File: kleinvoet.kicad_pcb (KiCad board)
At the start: 4 copper layers, 123 x 66 mm, 193 parts, among them J1 Conn_ST_STDC14, J11 Micro_SD_Card_Det, J12 JST-PH, J13 USB_C_Receptacle_USB2.0, J16 GPS_Transmission_Conn, J2 FTDI_Conn, J3 Sensor_Conn, J4 GPS_Transmission_Conn, J6 Sensor_Conn, Q1 PMOS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

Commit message: Fix KICAD! & DRC
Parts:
- moved TP8 7.68 mm to (138.5, 33.2)
- moved TP7 5.06 mm to (136.5, 33.2)
- moved TP11 2.75 mm to (138.5, 35.2)
- moved C66 2.75 mm to (65.1, 50.8)
- moved C64 2.10 mm to (69.3, 50.8)
- moved CB40 2.10 mm to (77.3, 61.4)
- moved D4 2.05 mm to (64.4, 48.2)
- moved BT1 1.95 mm to (66.3, 62.5)
- moved R3 1.95 mm to (72.7, 86.2)
- moved R4 1.95 mm to (59.7, 86.2)
- moved U11 1.95 mm to (66.2, 62.2)
- moved D3 1.95 mm to (64.0, 86.2)
- moved D2 1.95 mm to (68.4, 86.2)
- moved FB10 1.95 mm to (68.1, 73.5)
- moved C65 1.90 mm to (77.2, 65.2)
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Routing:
- net /~RST: track 147.3 -> 120.9 mm, vias 5 -> 4
- net /GNSS_Module/GPS_SYNC: track 2.75 -> 28.3 mm, vias 0 -> 1
- net Earth: track 103.7 -> 82.2 mm, vias 4 -> 0
- net /GNSS_Module/GPS_RX: track 14.4 -> 34.8 mm, vias 0 -> 1
- net Net-(U11-Pad12): track 13.2 -> 0.00 mm, vias 1 -> 0
- net /A0: track 45.5 -> 34.3 mm
- net +3V3: track 57.2 -> 65.7 mm, vias 68 -> 69
- net /A4: track 39.3 -> 44.8 mm
- net Net-(BT1-Pad1): track 43.0 -> 37.7 mm
- net /ADC_SAI_FS: track 37.3 -> 42.1 mm
- net Net-(FB10-Pad2): track 0.00 -> 3.58 mm
- net GND: track 209.0 -> 207.5 mm, vias 406 -> 403
- net /ADC_CTRL_SDA: track 38.6 -> 39.9 mm
- net Net-(D2-Pad2): track 3.80 -> 2.52 mm, vias 1 -> 0
- net /ADC_SAI_BCLK: track 28.9 -> 29.9 mm
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- removed copper zone on B.Cu, net (none)
- removed copper zone on In1.Cu, net (none)
- removed copper zone on In2.Cu, net (none)
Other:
- board text added: "+"
- board text added: "0"
- board text added: "1"
- board text added: "3v3ADC"
- board text added: "ADR0"
- board text added: "ADR1"
- board text added: "BCLK"
- board text added: "CH1"
- board text added: "CH2"
- board text added: "SAI_FS"
- board text added: "SAI_SD_A"
- board text added: "SAI_SD_B"
- board text added: "SCL"
- board text added: "SDA"
- board text added: "SD_CD"
- board text added: "VCM"
- board text removed: "ADC PORT"
- board text removed: "BL"
- board text removed: "BR"
- board text removed: "CEN"
- board text removed: "EN"
- board text removed: "GR"
- board text removed: "OR"
- board text removed: "SEN"
- board text removed: "SGN"
- board text removed: "SGP"
- board text removed: "SIG"

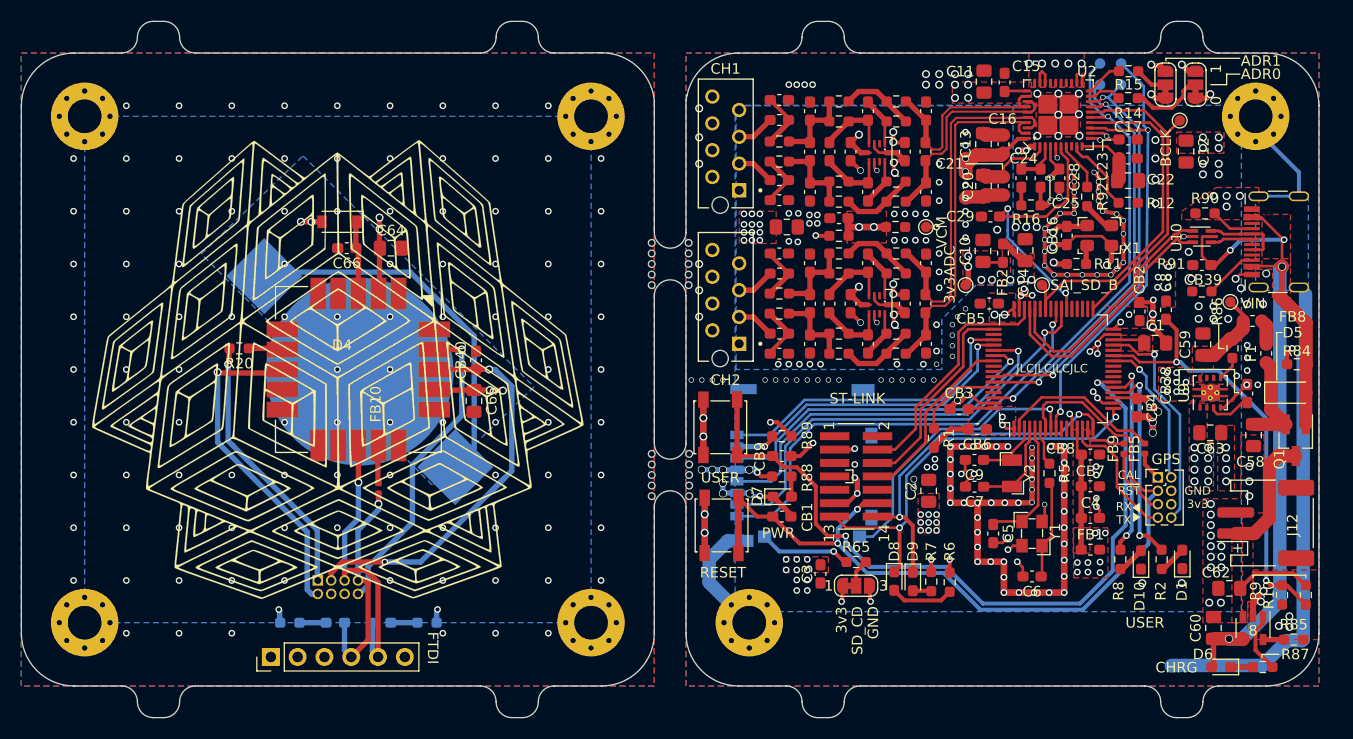
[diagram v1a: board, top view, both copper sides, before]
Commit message: Ready for panelisation
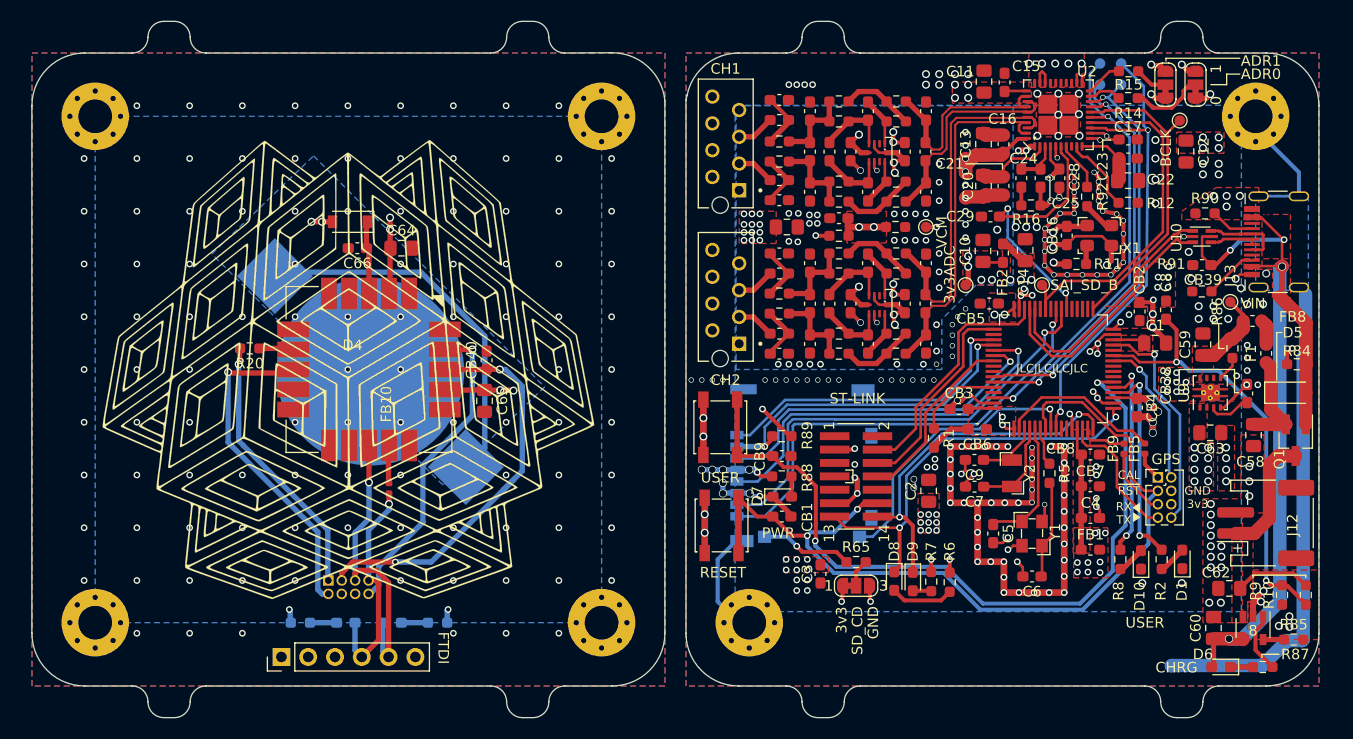
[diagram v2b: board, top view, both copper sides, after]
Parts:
- removed REF** (x4): Panel_Holes_6mm, grootvoet:Panel_Holes_6mm
- BT1: footprint Battery:BatteryHolder_Keystone_3002_1x2032 -> grootvoet:BatteryHolder_Keystone_3002_1x2032
- moved BT1 1.00 mm to (67.3, 62.5)
- moved C64 1.00 mm to (70.3, 50.8)
- moved C65 1.00 mm to (78.2, 65.2)
- moved C66 1.00 mm to (66.1, 50.8)
- moved CB40 1.00 mm to (78.3, 61.4)
- moved D2 1.00 mm to (69.4, 86.2)
- moved D3 1.00 mm to (65.0, 86.2)
- moved D4 1.00 mm to (65.4, 48.2)
- moved FB10 1.00 mm to (69.1, 73.5)
- moved G*** 1.00 mm to (79.2, 47.4)
- moved G*** 1.00 mm to (65.3, 62.2)
- moved G*** 1.00 mm to (43.0, 51.0)
- moved H13 1.00 mm to (89.2, 38.2)
- moved H14 1.00 mm to (41.2, 38.2)
- moved H15 1.00 mm to (89.2, 86.2)
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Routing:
- net GND: track 207.5 -> 204.8 mm, vias 403 -> 396
- net /~RST: track 120.9 -> 123.2 mm
- net /D12: track 71.6 -> 72.9 mm
- net +3V3: track 65.7 -> 66.9 mm
- net /SDIO_D3: track 33.6 -> 34.6 mm
- net /SDIO_D1: track 43.2 -> 43.9 mm
- net Earth: track 82.2 -> 81.5 mm
- net /SDIO_D0: track 42.4 -> 43.0 mm
- net /SDIO_CMD: track 33.1 -> 33.7 mm
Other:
- board size 123 x 66 mm -> 122 x 66 mm
- rule trace_min: 0.15 -> 0.2
- board text removed: "CUT OUT"

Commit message: Misc. changes
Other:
- board text added: "REV. B"
- board text added: "RXD"
- board text added: "TXD"
- board text removed: "WAKE"
- board text removed: "~BOOT"
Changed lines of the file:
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@@
   (general
     (thickness 1.6)
-    (drawings 188)
+    (drawings 189)
     (tracks 1715)
     (zones 0)
@@
   )
   (layers
-    (0 F.Cu signal)
-    (1 In1.Cu power)
-    (2 In2.Cu power)
-    (31 B.Cu signal)
-    (32 B.Adhes user)
-    (33 F.Adhes user)
-    (34 B.Paste user)
-    (35 F.Paste user)
+    (0 F.Cu signal hide)
+    (1 In1.Cu power hide)
+    (2 In2.Cu power hide)
+    (31 B.Cu signal hide)
+    (32 B.Adhes user hide)
+    (33 F.Adhes user hide)
+    (34 B.Paste user hide)
+    (35 F.Paste user hide)
     (36 B.SilkS user)
-    (37 F.SilkS user)
+    (37 F.SilkS user hide)
     (38 B.Mask user)
-    (39 F.Mask user)
-    (40 Dwgs.User user)
-    (41 Cmts.User user)
-    (42 Eco1.User user)
-    (43 Eco2.User user)
+    (39 F.Mask user hide)
+    (40 Dwgs.User user hide)
+    (41 Cmts.User user hide)
+    (42 Eco1.User user hide)
+    (43 Eco2.User user hide)
     (44 Edge.Cuts user)
-    (45 Margin user)
+    (45 Margin user hide)
     (46 B.CrtYd user)
-    (47 F.CrtYd user)
-    (48 B.Fab user)
-    (49 F.Fab user)
+    (47 F.CrtYd user hide)
+    (48 B.Fab user hide)
+    (49 F.Fab user hide)
   )
   (setup
@@
     (tags "BR2016 CR2016 DL2016 BR2020 CL2020 BR2025 CR2025 DL2025 DR2032 CR2032 DL2032")
     (attr smd)
-    (fp_text reference BT1 (at -9.15 -9.7 135) (layer B.SilkS)
+    (fp_text reference BT1 (at -9.15 -9.7 135) (layer B.SilkS) hide
       (effects (font (size 1 1) (thickness 0.15)) (justify mirror))
     )
@@
   (module grootvoet:microSD_HC_Molex_5031821852 (layer B.Cu)
     (at 101.45 63.65 270)
-    (fp_text reference J11 (at 7.8 -17.5 90) (layer B.SilkS)
+    (fp_text reference J11 (at 7.8 -17.5 90) (layer B.SilkS) hide
       (effects (font (size 1 1) (thickness 0.15)) (justify mirror))
     )
@@
     (tags "resistor handsolder")
     (attr smd)
-    (fp_text reference R20 (at 0 -1.43) (layer F.SilkS)
+    (fp_text reference R20 (at 0 -1.43) (layer F.SilkS) hide
       (effects (font (size 1 1) (thickness 0.15)))
     )
@@
     (tags "resistor handsolder")
     (attr smd)
-    (fp_text reference R4 (at 0 1.43) (layer B.SilkS)
+    (fp_text reference R4 (at 0 -1.6 270 unlocked) (layer B.SilkS)
       (effects (font (size 1 1) (thickness 0.15)) (justify mirror))
     )
@@
     (tags "resistor handsolder")
     (attr smd)
-    (fp_text reference R3 (at 0 1.43) (layer B.SilkS)
+    (fp_text reference R3 (at -0.15 1.8 270 unlocked) (layer B.SilkS)
       (effects (font (size 1 1) (thickness 0.15)) (justify mirror))
     )
@@
     (tags "capacitor handsolder")
     (attr smd)
-    (fp_text reference C65 (at 0 -1.68 90) (layer F.SilkS)
+    (fp_text reference C65 (at 0 -1.68 90) (layer F.SilkS) hide
       (effects (font (size 1 1) (thickness 0.15)))
     )
@@
     (tags "capacitor handsolder")
     (attr smd)
-    (fp_text reference C64 (at 0 -1.68) (layer F.SilkS)
+    (fp_text reference C64 (at 0 -1.68) (layer F.SilkS) hide
       (effects (font (size 1 1) (thickness 0.15)))
     )
@@
     (tags "capacitor handsolder")
     (attr smd)
-    (fp_text reference CB40 (at 0 -1.43 90) (layer F.SilkS)
+    (fp_text reference CB40 (at 0 -1.43 90) (layer F.SilkS) hide
       (effects (font (size 1 1) (thickness 0.15)))
     )
@@
     (tags "capacitor handsolder")
     (attr smd)
-    (fp_text reference C66 (at 0 -1.43) (layer F.SilkS)
+    (fp_text reference C66 (at 0 -1.43) (layer F.SilkS) hide
       (effects (font (size 1 1) (thickness 0.15)))
     )
@@
     (tags "LED handsolder")
     (attr smd)
-    (fp_text reference D3 (at 2.361666 0.05) (layer B.SilkS)
+    (fp_text reference D3 (at -0.446666 -1.8 270 unlocked) (layer B.SilkS)
       (effects (font (size 1 1) (thickness 0.15)) (justify mirror))
     )
@@
     (tags "LED handsolder")
     (attr smd)
-    (fp_text reference D2 (at 2.361668 -0.05) (layer B.SilkS)
+    (fp_text reference D2 (at -0.146667 -1.8 270 unlocked) (layer B.SilkS)
       (effects (font (size 1 1) (thickness 0.15)) (justify mirror))
     )
@@
     (tags inductor)
     (attr smd)
-    (fp_text reference FB10 (at 7.983 -0.254 270) (layer F.SilkS)
+    (fp_text reference FB10 (at 7.983 -0.254 270) (layer F.SilkS) hide
       (effects (font (size 1 1) (thickness 0.15)))
     )
@@
     (tags SOD-123)
     (attr smd)
-    (fp_text reference D4 (at -0.244 -11.694) (layer F.SilkS)
+    (fp_text reference D4 (at -0.244 -11.694) (layer F.SilkS) hide
       (effects (font (size 1 1) (thickness 0.15)))
     )
@@
     )
   )
+  (gr_line (start 153.25 73.05) (end 157.25 73.05) (layer B.SilkS) (width 0.12))
+  (gr_line (start 153.25 80.05) (end 153.25 73.05) (layer B.SilkS) (width 0.12))
+  (gr_line (start 157.25 80.05) (end 153.25 80.05) (layer B.SilkS) (width 0.12))
+  (gr_poly (pts (xy 66.75 87) (xy 65.95 87) (xy 66.35 87.6)) (layer F.SilkS) (width 0.1))
+  (gr_poly (pts (xy 68.6 87.6) (xy 69.4 87.6) (xy 69 87)) (layer F.SilkS) (width 0.1))
+  (gr_text "REV. B" (at 128.25 90.25) (layer F.SilkS)
+    (effects (font (size 1 1) (thickness 0.25)))
+  )
   (gr_text + (at 149.55 79.15) (layer F.SilkS)
     (effects (font (size 1 1) (thickness 0.25)))
@@
     (effects (font (size 0.8 0.8) (thickness 0.15)))
   )
-  (gr_text ~BOOT (at 64.55 81.592858 270) (layer B.SilkS)
-    (effects (font (size 0.8 0.8) (thickness 0.15)) (justify mirror))
-  )
-  (gr_text 3v3 (at 60.75 82.069048 270) (layer B.SilkS)
-    (effects (font (size 0.8 0.8) (thickness 0.15)) (justify mirror))
-  )
-  (gr_text GND (at 61.95 81.916667 270) (layer B.SilkS)
-    (effects (font (size 0.8 0.8) (thickness 0.15)) (justify mirror))
-  )
-  (gr_text WAKE (at 68.55 81.57381 270) (layer B.SilkS)
-    (effects (font (size 0.8 0.8) (thickness 0.15)) (justify mirror))
-  )
-  (gr_text "VBAT : CR2032" (at 52.75 70.25 270) (layer B.SilkS)
+  (gr_text "VBAT : CR2032" (at 76.05 53.85 315) (layer B.SilkS)
     (effects (font (size 1 1) (thickness 0.15)) (justify mirror))
   )
@@
     (effects (font (size 1 1) (thickness 0.15)))
   )
-  (gr_text TX (at 55.25 89.65 180) (layer B.SilkS)
-    (effects (font (size 1 1) (thickness 0.15)) (justify mirror))
-  )
-  (gr_text RX (at 75.05 89.75 180) (layer B.SilkS)
-    (effects (font (size 1 1) (thickness 0.15)) (justify mirror))
+  (gr_text TXD (at 68.85 85.45 270) (layer F.SilkS)
+    (effects (font (size 1 1) (thickness 0.15)))
   )
-  (gr_poly (pts (xy 62.85 83.65) (xy 63.65 83.65) (xy 63.25 84.25)) (layer B.SilkS) (width 0.1))
-  (gr_text SYNC (at 63.25 81.592858 270) (layer B.SilkS)
-    (effects (font (size 0.8 0.8) (thickness 0.15)) (justify mirror))
+  (gr_text RXD (at 66.25 85.45 270) (layer F.SilkS)
+    (effects (font (size 1 1) (thickness 0.15)))
   )
-  (gr_poly (pts (xy 67.65 84.25) (xy 66.85 84.25) (xy 67.25 83.65)) (layer B.SilkS) (width 0.1))
-  (gr_text TX (at 67.25 82.45 270) (layer B.SilkS)
+  (gr_poly (pts (xy 62.85 80.25) (xy 63.65 80.25) (xy 63.25 80.85)) (layer B.SilkS) (width 0.1))
+  (gr_text SYNC (at 63.25 78.45 270) (layer B.SilkS)
     (effects (font (size 0.8 0.8) (thickness 0.15)) (justify mirror))
   )
-  (gr_poly (pts (xy 65.45 83.65) (xy 66.25 83.65) (xy 65.85 84.25)) (layer B.SilkS) (width 0.1))
-  (gr_text RX (at 65.85 82.354762 270) (layer B.SilkS)
+  (gr_poly (pts (xy 67.65 80.85) (xy 66.85 80.85) (xy 67.25 80.25)) (layer B.SilkS) (width 0.1))
+  (gr_text TXD (at 66.05 78.85 270) (layer B.SilkS)
     (effects (font (size 0.8 0.8) (thickness 0.15)) (justify mirror))
   )
-  (gr_text ~RST (at 69.65 82.05 270) (layer B.SilkS)
+  (gr_poly (pts (xy 65.5 80.25) (xy 66.3 80.25) (xy 65.9 80.85)) (layer B.SilkS) (width 0.1))
+  (gr_text RXD (at 67.25 78.85 270) (layer B.SilkS)
     (effects (font (size 0.8 0.8) (thickness 0.15)) (justify mirror))
   )

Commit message: Update pinout
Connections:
- CB9 pad 1: /D12 -> /D11
- R2 pad 2: /A2 -> /D13
- R8 pad 2: /D13 -> /D12
- SW2 pad 1: /D12 -> /D11
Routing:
- net /D11: track 0.00 -> 73.2 mm, vias 0 -> 2
- net /D12: track 72.9 -> 18.9 mm
- net /A2: track 19.7 -> 0.00 mm, vias 2 -> 0

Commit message: Reference panel
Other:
- board outline removed
